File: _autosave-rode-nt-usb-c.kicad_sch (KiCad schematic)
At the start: 8 parts, among them J1 USB_C_Receptacle, J2 Conn_01x05_Pin, J3 USB_C_Receptacle_USB2.0_16P

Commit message: Change usb side
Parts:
- removed J1: USB_C_Receptacle, Connector_USB:USB_C_Receptacle_GCT_USB4105-xx-A_16P_TopMnt_Horizontal, symbol Connector:USB_C_Receptacle
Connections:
- no-connect marks 12 -> 2
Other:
- moved on the sheet: D1, J2, J3, R1, R2, R3, R4

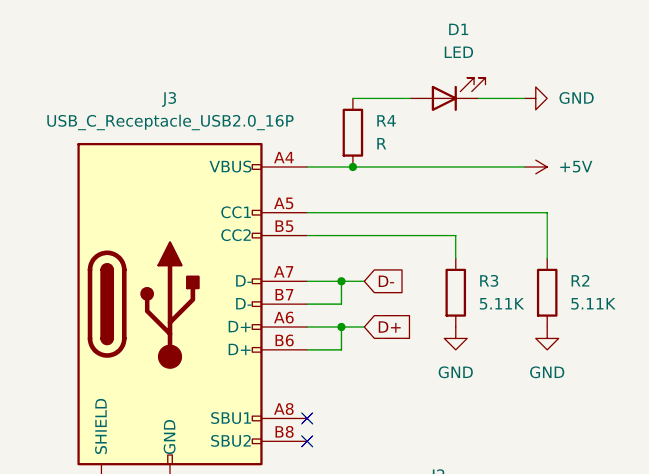
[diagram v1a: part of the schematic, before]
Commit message: Add 3d insert model, change pcb
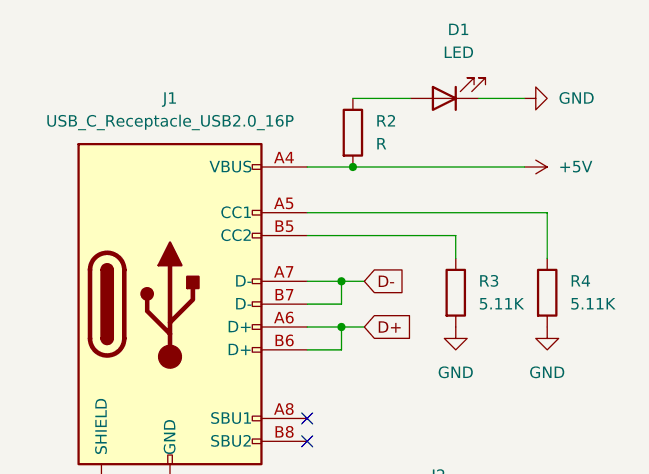
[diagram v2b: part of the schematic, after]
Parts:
- renumbered J3 to J1, R4 to R2, R2 to R4
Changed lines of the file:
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@@
 		(dnp no)
 		(fields_autoplaced yes)
-		(property "Reference" "R2"
+		(property "Reference" "R4"
 			(at 130.81 83.8199 0)
 			(effects
@@
 			(project "rode-nt-usb-c"
 				(path "/65483df2-e61e-4f34-9202-fac169fa34d7"
-					(reference "R2")
+					(reference "R4")
 					(unit 1)
 				)
@@
 		(dnp no)
 		(fields_autoplaced yes)
-		(property "Reference" "J3"
+		(property "Reference" "J1"
 			(at 86.36 63.5 0)
 			(effects
@@
 			(project ""
 				(path "/65483df2-e61e-4f34-9202-fac169fa34d7"
-					(reference "J3")
+					(reference "J1")
 					(unit 1)
 				)
@@
 		(dnp no)
 		(fields_autoplaced yes)
-		(property "Reference" "R4"
+		(property "Reference" "R2"
 			(at 109.22 66.0399 0)
 			(effects
@@
 			(project "rode-nt-usb-c"
 				(path "/65483df2-e61e-4f34-9202-fac169fa34d7"
-					(reference "R4")
-					(unit 1)
-				)
+					(reference "R2")
+					(unit 1)
+				)
